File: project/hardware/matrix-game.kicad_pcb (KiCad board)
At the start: 2 copper layers, 11 parts, among them SW1 button_center, SW2 button_left, SW3 button_down, SW4 button_right, SW5 button_up, U1 NUCLEO-F042K6, U2 MAX7219, U3 SSD1306

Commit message: [project/hardware/layout] added custom footprint for LCD
Signed-off-by: Timon Burkard <timon.burkard@gwf.ch>
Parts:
- U3: footprint Connector_PinSocket_2.54mm:PinSocket_1x04_P2.54mm_Vertical -> Custom_Library:LCD_I2C
- moved U3 26.9 mm to (195.0, 121.0)
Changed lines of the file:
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@@
 		)
 	)
-	(footprint "Connector_PinSocket_2.54mm:PinSocket_1x04_P2.54mm_Vertical"
+	(footprint "Custom_Library:LCD_I2C"
 		(layer "F.Cu")
-		(at 168.09 120.35)
-		(descr "Through hole straight socket strip, 1x04, 2.54mm pitch, single row (from Kicad 4.0.7), script generated")
-		(tags "Through hole socket strip THT 1x04 2.54mm single row")
+		(at 195 121)
 		(property "Reference" "U3"
-			(at 0 -2.77 0)
-			(layer "F.SilkS")
-			(effects
-				(font
-					(size 1 1)
-					(thickness 0.15)
+			(at 0 -0.5 0)
+			(unlocked yes)
+			(layer "F.SilkS")
+			(effects
+				(font
+					(size 1 1)
+					(thickness 0.1)
 				)
 			)
 		)
 		(property "Value" "SSD1306"
-			(at 0 10.39 0)
-			(layer "F.Fab")
-			(effects
-				(font
-					(size 1 1)
-					(thickness 0.15)
-				)
-			)
-		)
-		(property "Footprint" "Connector_PinSocket_2.54mm:PinSocket_1x04_P2.54mm_Vertical"
+			(at 0 1 0)
+			(unlocked yes)
+			(layer "F.Fab")
+			(effects
+				(font
+					(size 1 1)
+					(thickness 0.15)
+				)
+			)
+		)
+		(property "Footprint" "Custom_Library:LCD_I2C"
 			(at 0 0 0)
 			(unlocked yes)
@@
 			(effects
 				(font
-					(size 1.27 1.27)
+					(size 1 1)
 					(thickness 0.15)
 				)
@@
 			(effects
 				(font
-					(size 1.27 1.27)
+					(size 1 1)
 					(thickness 0.15)
 				)
@@
 			(effects
 				(font
-					(size 1.27 1.27)
+					(size 1 1)
 					(thickness 0.15)
 				)
@@
 		(attr through_hole)
 		(fp_line
-			(start -1.33 1.27)
-			(end -1.33 8.95)
-			(stroke
-				(width 0.12)
-				(type solid)
-			)
-			(layer "F.SilkS")
-		)
-		(fp_line
-			(start -1.33 1.27)
-			(end 1.33 1.27)
-			(stroke
-				(width 0.12)
-				(type solid)
-			)
-			(layer "F.SilkS")
-		)
-		(fp_line
-			(start -1.33 8.95)
-			(end 1.33 8.95)
-			(stroke
-				(width 0.12)
-				(type solid)
-			)
-			(layer "F.SilkS")
-		)
-		(fp_line
-			(start 0 -1.33)
-			(end 1.33 -1.33)
-			(stroke
-				(width 0.12)
-				(type solid)
-			)
-			(layer "F.SilkS")
-		)
-		(fp_line
-			(start 1.33 -1.33)
-			(end 1.33 0)
-			(stroke
-				(width 0.12)
-				(type solid)
-			)
-			(layer "F.SilkS")
-		)
-		(fp_line
-			(start 1.33 1.27)
-			(end 1.33 8.95)
-			(stroke
-				(width 0.12)
-				(type solid)
-			)
-			(layer "F.SilkS")
-		)
-		(fp_line
-			(start -1.8 -1.8)
-			(end 1.75 -1.8)
-			(stroke
-				(width 0.05)
-				(type solid)
-			)
-			(layer "F.CrtYd")
-		)
-		(fp_line
-			(start -1.8 9.4)
-			(end -1.8 -1.8)
-			(stroke
-				(width 0.05)
-				(type solid)
-			)
-			(layer "F.CrtYd")
-		)
-		(fp_line
-			(start 1.75 -1.8)
-			(end 1.75 9.4)
-			(stroke
-				(width 0.05)
-				(type solid)
-			)
-			(layer "F.CrtYd")
-		)
-		(fp_line
-			(start 1.75 9.4)
-			(end -1.8 9.4)
-			(stroke
-				(width 0.05)
-				(type solid)
-			)
-			(layer "F.CrtYd")
-		)
-		(fp_line
-			(start -1.27 -1.27)
-			(end 0.635 -1.27)
-			(stroke
-				(width 0.1)
-				(type solid)
-			)
-			(layer "F.Fab")
-		)
-		(fp_line
-			(start -1.27 8.89)
-			(end -1.27 -1.27)
-			(stroke
-				(width 0.1)
-				(type solid)
-			)
-			(layer "F.Fab")
-		)
-		(fp_line
-			(start 0.635 -1.27)
-			(end 1.27 -0.635)
-			(stroke
-				(width 0.1)
-				(type solid)
-			)
-			(layer "F.Fab")
-		)
-		(fp_line
-			(start 1.27 -0.635)
-			(end 1.27 8.89)
-			(stroke
-				(width 0.1)
-				(type solid)
-			)
-			(layer "F.Fab")
-		)
-		(fp_line
-			(start 1.27 8.89)
-			(end -1.27 8.89)
-			(stroke
-				(width 0.1)
-				(type solid)
-			)
-			(layer "F.Fab")
+			(start -13 -12)
+			(end 13 -12)
+			(stroke
+				(width 0.1)
+				(type default)
+			)
+			(layer "F.SilkS")
+		)
+		(fp_line
+			(start -13 14)
+			(end -13 -12)
+			(stroke
+				(width 0.1)
+				(type default)
+			)
+			(layer "F.SilkS")
+		)
+		(fp_line
+			(start 13 -12)
+			(end 13 14)
+			(stroke
+				(width 0.1)
+				(type default)
+			)
+			(layer "F.SilkS")
+		)
+		(fp_line
+			(start 13 14)
+			(end -13 14)
+			(stroke
+				(width 0.1)
+				(type default)
+			)
+			(layer "F.SilkS")
+		)
+		(fp_text user "SCL"
+			(at 1.778 -6.604 90)
+			(unlocked yes)
+			(layer "F.SilkS")
+			(effects
+				(font
+					(size 0.7 0.7)
+					(thickness 0.15)
+					(bold yes)
+				)
+				(justify left bottom)
+			)
+		)
+		(fp_text user "SDA"
+			(at 4.318 -6.604 90)
+			(unlocked yes)
+			(layer "F.SilkS")
+			(effects
+				(font
+					(size 0.7 0.7)
+					(thickness 0.15)
+					(bold yes)
+				)
+				(justify left bottom)
+			)
+		)
+		(fp_text user "GND"
+			(at -3.302 -6.35 90)
+			(unlocked yes)
+			(layer "F.SilkS")
+			(effects
+				(font
+					(size 0.7 0.7)
+					(thickness 0.15)
+					(bold yes)
+				)
+				(justify left bottom)
+			)
+		)
+		(fp_text user "VCC"
+			(at -0.762 -6.35 90)
+			(unlocked yes)
+			(layer "F.SilkS")
+			(effects
+				(font
+					(size 0.7 0.7)
+					(thickness 0.15)
+					(bold yes)
+				)
+				(justify left bottom)
+			)
 		)
 		(fp_text user "${REFERENCE}"
-			(at 0 3.81 90)
+			(at 0 2.5 0)
+			(unlocked yes)
 			(layer "F.Fab")
 			(effects
@@
 		)
 		(pad "1" thru_hole rect
-			(at 0 0)
-			(size 1.7 1.7)
-			(drill 1)
+			(at -3.81 -10.16)
+			(size 1.524 1.524)
+			(drill 0.762)
 			(layers "*.Cu" "*.Mask")
 			(remove_unused_layers no)
@@
 			(pintype "input")
 		)
-		(pad "2" thru_hole oval
-			(at 0 2.54)
-			(size 1.7 1.7)
-			(drill 1)
+		(pad "2" thru_hole circle
+			(at -1.27 -10.16)
+			(size 1.524 1.524)
+			(drill 0.762)
 			(layers "*.Cu" "*.Mask")
 			(remove_unused_layers no)
@@
 			(pintype "input")
 		)
-		(pad "3" thru_hole oval
-			(at 0 5.08)
-			(size 1.7 1.7)
-			(drill 1)
+		(pad "3" thru_hole circle
+			(at 1.27 -10.16)
+			(size 1.524 1.524)
+			(drill 0.762)
 			(layers "*.Cu" "*.Mask")
 			(remove_unused_layers no)
@@
 			(pintype "input")
 		)
-		(pad "4" thru_hole oval
-			(at 0 7.62)
-			(size 1.7 1.7)
-			(drill 1)
+		(pad "4" thru_hole circle
+			(at 3.81 -10.16)
+			(size 1.524 1.524)
+			(drill 0.762)
 			(layers "*.Cu" "*.Mask")
 			(remove_unused_layers no)
@@
 			(pintype "input")
 		)
-		(model "${KICAD8_3DMODEL_DIR}/Connector_PinSocket_2.54mm.3dshapes/PinSocket_1x04_P2.54mm_Vertical.wrl"
-			(offset
-				(xyz 0 0 0)
-			)
-			(scale
-				(xyz 1 1 1)
-			)
-			(rotate
-				(xyz 0 0 0)
-			)
-		)
+		(zone
+			(net 0)
+			(net_name "")
+			(layer "F.SilkS")
+			(hatch edge 0.5)
+			(connect_pads
+				(clearance 0)
+			)
+			(min_thickness 0.25)
+			(filled_areas_thickness no)
+			(keepout
+				(tracks allowed)
+				(vias allowed)
+				(pads not_allowed)
+				(copperpour allowed)
+				(footprints not_allowed)
+			)
+			(fill
+				(thermal_gap 0.5)
+				(thermal_bridge_width 0.5)
+			)
+			(polygon
+				(pts
+					(xy 182 109) (xy 208 109) (xy 208 135) (xy 182 135)
+				)
+			)
+		)

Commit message: [project/hardware/layout] started layouting
Signed-off-by: Timon Burkard <timon.burkard@gwf.ch>
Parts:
- moved SW2 96.3 mm to (112.0, 128.9), turned to 180 degrees
- moved SW1 94.7 mm to (126.0, 128.9), turned to 180 degrees
- moved SW3 90.7 mm to (119.5, 136.6)
- moved U3 67.3 mm to (170.8, 58.2)
- moved SW4 66.3 mm to (138.7, 128.9), turned to 180 degrees
- moved SW5 61.2 mm to (126.0, 117.5), turned to 180 degrees
- moved U1 31.3 mm to (178.6, 101.8), turned to 180 degrees
- moved U2 25.2 mm to (157.9, 77.5)
- moved BZ1 15.5 mm to (163.8, 121.9), turned to 180 degrees
- moved R1 5.16 mm to (166.1, 111.0), turned to 180 degrees
- moved D1 2.40 mm to (121.0, 76.0)
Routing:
- net Net-(U1-PA3/A2): track 0.00 -> 109.8 mm
- net +3.3V: track 0.00 -> 109.6 mm, vias 0 -> 28
- net Net-(U1-PB1/D6): track 0.00 -> 97.7 mm, vias 0 -> 1
- net Net-(D1-R3): track 0.00 -> 87.2 mm
- net Net-(D1-R5): track 0.00 -> 85.7 mm
- net Net-(D1-R7): track 0.00 -> 78.9 mm, vias 0 -> 1
- net Net-(U1-PA8/D9): track 0.00 -> 78.6 mm
- net Net-(D1-R6): track 0.00 -> 74.8 mm
- net Net-(U1-PB0/D3): track 0.00 -> 74.7 mm, vias 0 -> 1
- net Net-(D1-C2): track 0.00 -> 72.4 mm, vias 0 -> 1
- net Net-(D1-R8): track 0.00 -> 69.5 mm
- net Net-(U1-PA12/D2): track 0.00 -> 66.6 mm
- net Net-(D1-C3): track 0.00 -> 66.1 mm, vias 0 -> 3
- net Net-(D1-C5): track 0.00 -> 60.9 mm, vias 0 -> 2
- net Net-(U1-PA7/A6): track 0.00 -> 55.6 mm, vias 0 -> 1
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- added copper zone on B.Cu, net +3.3V
- added copper zone on F.Cu, net GND
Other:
- board outline added: 100 x 100 mm

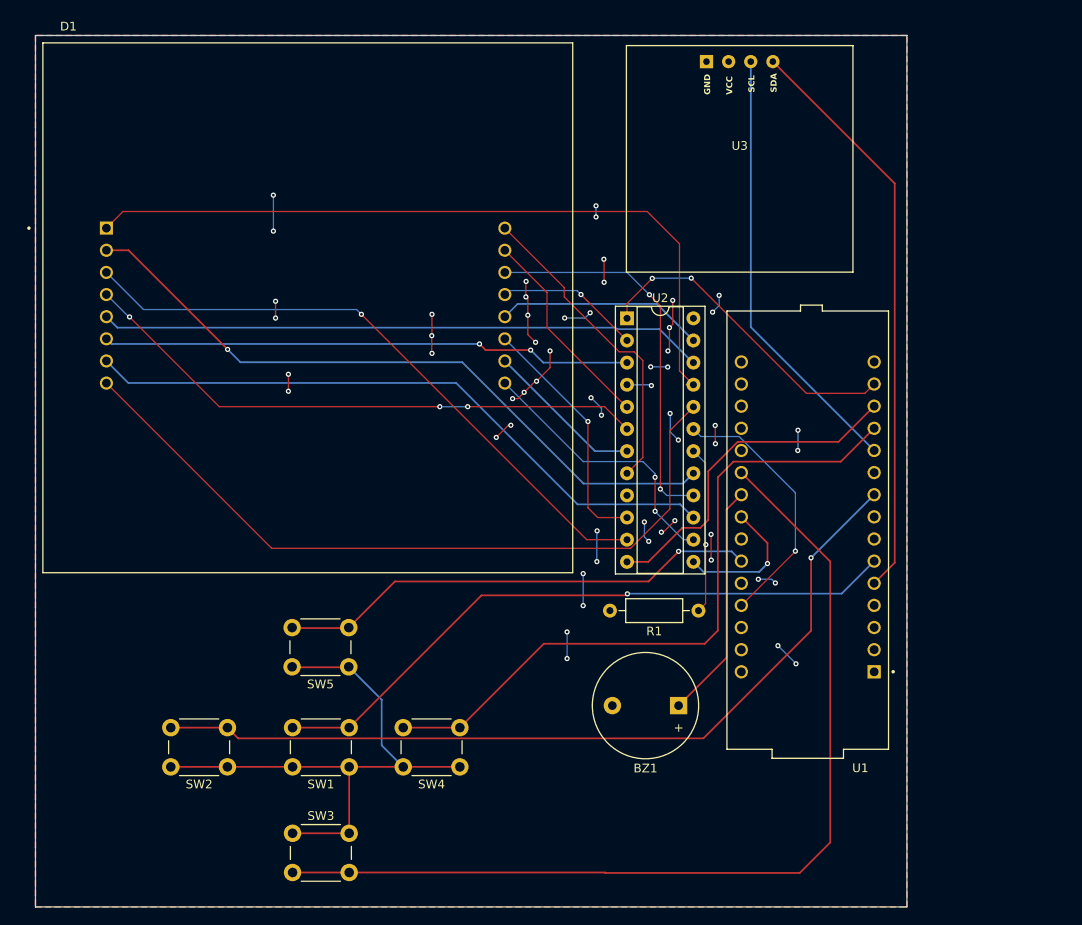
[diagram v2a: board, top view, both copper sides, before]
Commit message: [project/hardware/layout] set all tracks to 0.2 mm width
Signed-off-by: Timon Burkard <timon.burkard@gwf.ch>
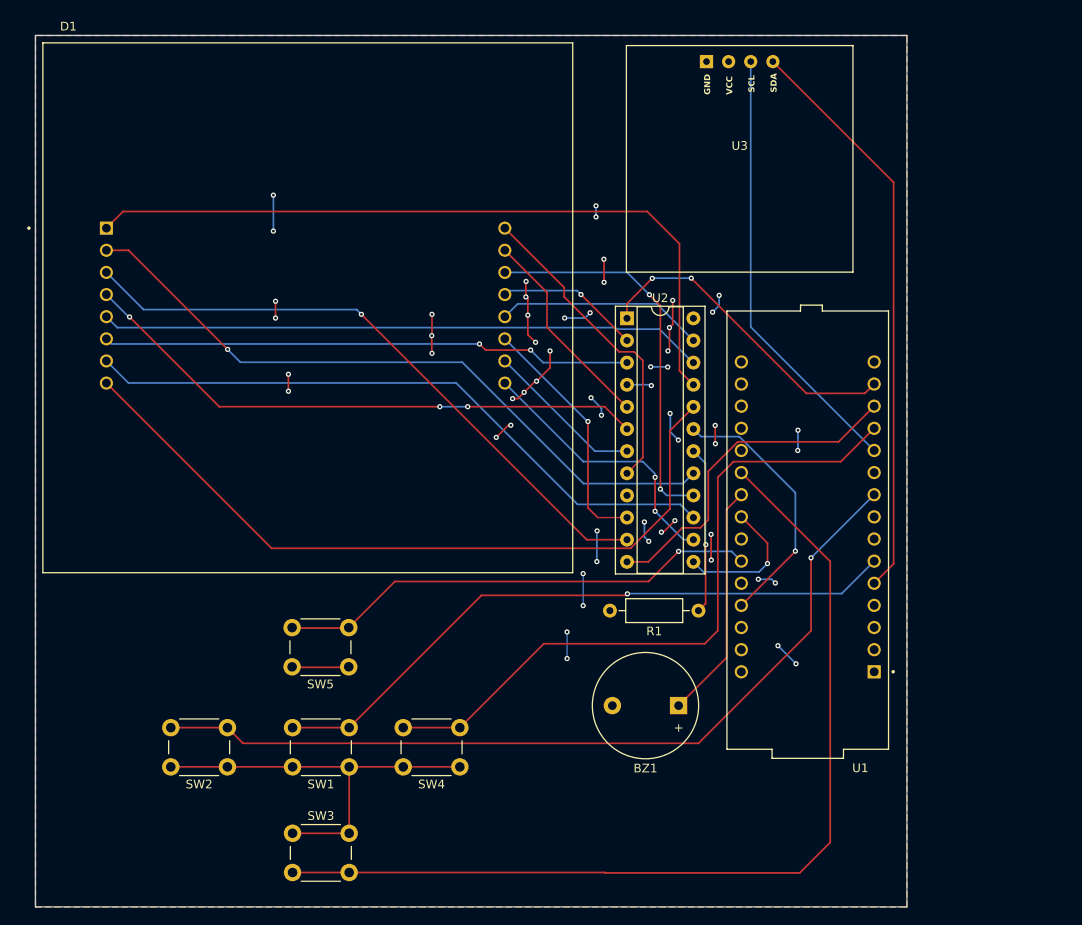
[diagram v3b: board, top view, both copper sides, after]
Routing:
- net +3.3V: track 109.6 -> 95.5 mm
- net Net-(D1-R5): track 85.7 -> 84.9 mm

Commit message: [project/hardware/layout] rotation of matrix LED
Signed-off-by: Timon Burkard <timon.burkard@gwf.ch>
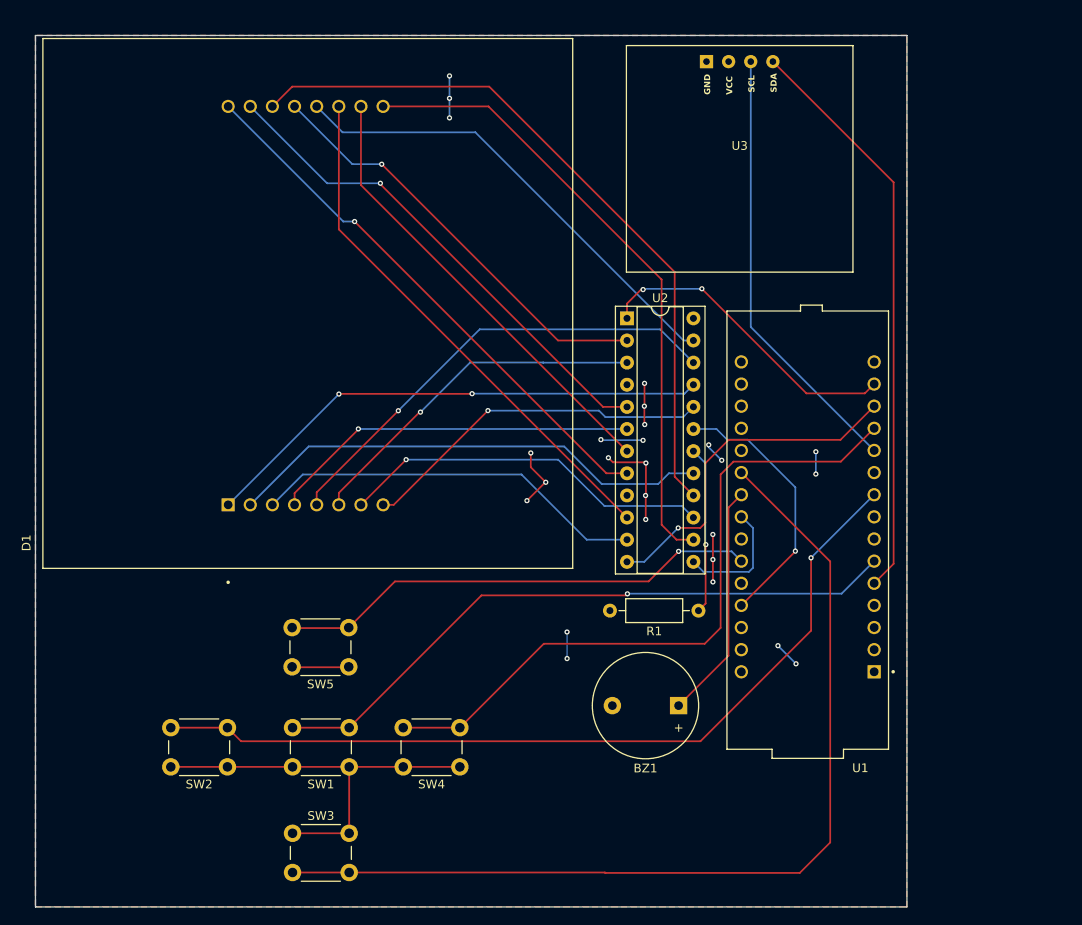
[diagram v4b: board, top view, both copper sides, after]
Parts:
- turned D1 to 90 degrees
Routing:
- net Net-(D1-R3): track 87.2 -> 40.9 mm, vias 0 -> 1
- net Net-(D1-R1): track 31.6 -> 72.7 mm, vias 2 -> 0
- net Net-(D1-R2): track 44.6 -> 82.4 mm, vias 2 -> 0
- net Net-(D1-C4): track 18.3 -> 52.2 mm
- net Net-(D1-C7): track 23.8 -> 57.6 mm, vias 0 -> 1
- net Net-(D1-C1): track 16.6 -> 49.3 mm
- net Net-(D1-C6): track 28.3 -> 60.9 mm, vias 1 -> 0
- net Net-(D1-R6): track 74.8 -> 43.1 mm, vias 0 -> 1
- net Net-(D1-R4): track 24.0 -> 54.4 mm
- net Net-(D1-C2): track 72.4 -> 45.2 mm, vias 1 -> 0
- net Net-(D1-C8): track 36.5 -> 63.2 mm, vias 0 -> 1
- net Net-(D1-R5): track 84.9 -> 59.1 mm, vias 0 -> 2
- net Net-(D1-C3): track 66.1 -> 42.6 mm, vias 3 -> 1
- net Net-(D1-R7): track 78.9 -> 55.9 mm, vias 1 -> 0
- net GND: track 41.6 -> 20.6 mm, vias 29 -> 13
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
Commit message: [project/hardware] added test points
Signed-off-by: Timon Burkard <timon.burkard@gwf.ch>
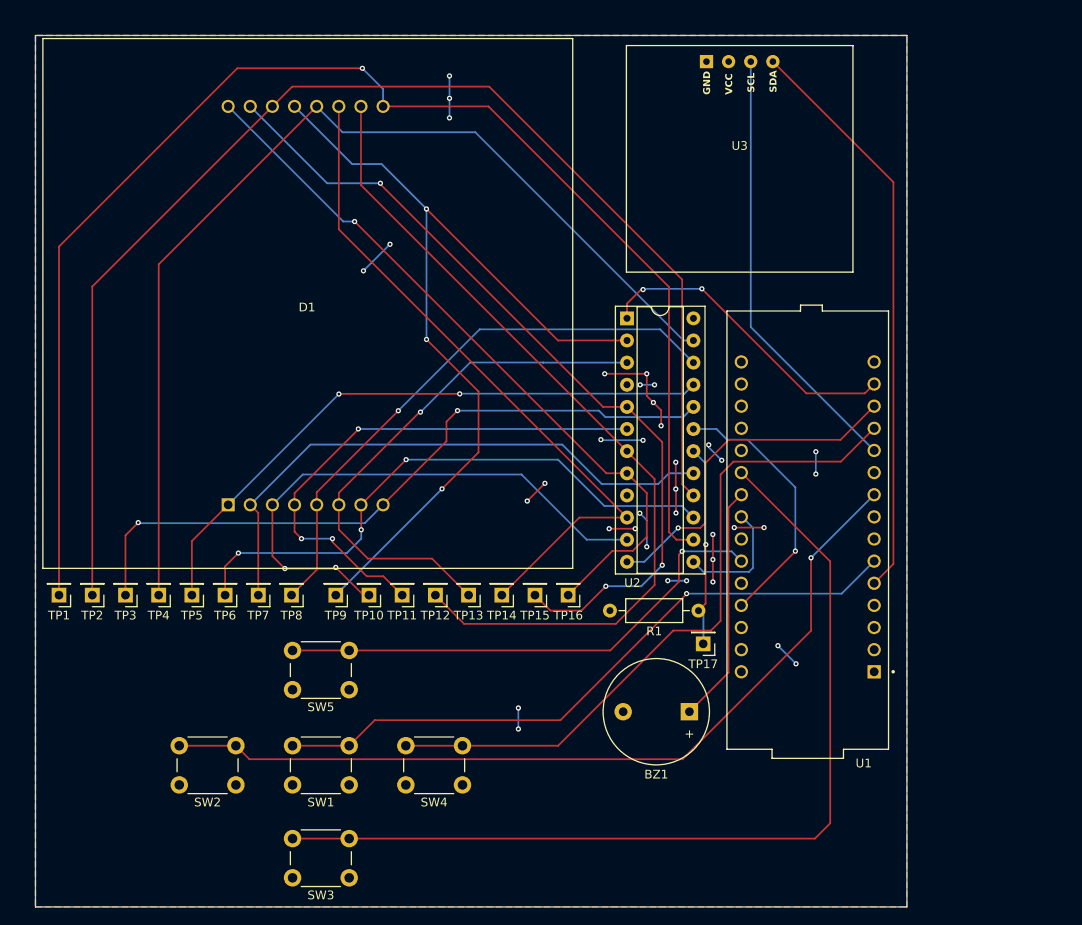
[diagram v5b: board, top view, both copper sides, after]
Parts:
- added TP1: TestPoint, Connector_PinHeader_2.54mm:PinHeader_1x01_P2.54mm_Vertical, F.Cu at (92.7, 109.2)
- added TP10: TestPoint, Connector_PinHeader_2.54mm:PinHeader_1x01_P2.54mm_Vertical, F.Cu at (128.3, 109.2)
- added TP11: TestPoint, Connector_PinHeader_2.54mm:PinHeader_1x01_P2.54mm_Vertical, F.Cu at (132.1, 109.2)
- added TP12: TestPoint, Connector_PinHeader_2.54mm:PinHeader_1x01_P2.54mm_Vertical, F.Cu at (135.9, 109.2)
- added TP13: TestPoint, Connector_PinHeader_2.54mm:PinHeader_1x01_P2.54mm_Vertical, F.Cu at (139.7, 109.2)
- added TP14: TestPoint, Connector_PinHeader_2.54mm:PinHeader_1x01_P2.54mm_Vertical, F.Cu at (143.5, 109.2)
- added TP15: TestPoint, Connector_PinHeader_2.54mm:PinHeader_1x01_P2.54mm_Vertical, F.Cu at (147.3, 109.2)
- added TP16: TestPoint, Connector_PinHeader_2.54mm:PinHeader_1x01_P2.54mm_Vertical, F.Cu at (151.1, 109.2)
- added TP17: TestPoint, Connector_PinHeader_2.54mm:PinHeader_1x01_P2.54mm_Vertical, F.Cu at (166.6, 114.8)
- added TP2: TestPoint, Connector_PinHeader_2.54mm:PinHeader_1x01_P2.54mm_Vertical, F.Cu at (96.5, 109.2)
- added TP3: TestPoint, Connector_PinHeader_2.54mm:PinHeader_1x01_P2.54mm_Vertical, F.Cu at (100.3, 109.2)
- added TP4: TestPoint, Connector_PinHeader_2.54mm:PinHeader_1x01_P2.54mm_Vertical, F.Cu at (104.1, 109.2)
- added TP5: TestPoint, Connector_PinHeader_2.54mm:PinHeader_1x01_P2.54mm_Vertical, F.Cu at (108.0, 109.2)
- added TP6: TestPoint, Connector_PinHeader_2.54mm:PinHeader_1x01_P2.54mm_Vertical, F.Cu at (111.8, 109.2)
- added TP7: TestPoint, Connector_PinHeader_2.54mm:PinHeader_1x01_P2.54mm_Vertical, F.Cu at (115.6, 109.2)
- added TP8: TestPoint, Connector_PinHeader_2.54mm:PinHeader_1x01_P2.54mm_Vertical, F.Cu at (119.4, 109.2)
- added TP9: TestPoint, Connector_PinHeader_2.54mm:PinHeader_1x01_P2.54mm_Vertical, F.Cu at (124.5, 109.2)
- moved SW3 8.27 mm to (126.0, 141.7), turned to 180 degrees
- moved SW5 2.62 mm to (126.0, 120.1)
- moved SW2 2.29 mm to (113.0, 131.0)
- moved SW4 2.09 mm to (139.0, 131.0)
- moved SW1 2.07 mm to (126.0, 131.0)
- moved BZ1 1.42 mm to (165.0, 122.6)
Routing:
- net Net-(D1-R1): track 72.7 -> 161.3 mm, vias 0 -> 1
- net Net-(D1-R2): track 82.4 -> 147.1 mm
- net Net-(D1-R4): track 54.4 -> 117.9 mm
- net Net-(D1-C1): track 49.3 -> 102.9 mm, vias 1 -> 3
- net +3.3V: track 82.2 -> 32.1 mm, vias 13 -> 16
- net Net-(D1-C4): track 52.2 -> 97.3 mm
- net Net-(D1-R3): track 40.9 -> 80.2 mm, vias 1 -> 2
- net Net-(D1-C7): track 57.6 -> 95.0 mm, vias 1 -> 3
- net Net-(D1-R6): track 43.1 -> 67.2 mm, vias 1 -> 3
- net Net-(D1-C5): track 40.6 -> 61.5 mm
- net Net-(D1-C8): track 63.2 -> 83.2 mm
- net Net-(D1-C2): track 45.2 -> 64.2 mm, vias 0 -> 2
- net Net-(D1-C3): track 42.6 -> 61.3 mm, vias 1 -> 3
- net Net-(D1-C6): track 60.9 -> 78.9 mm
- net Net-(D1-R5): track 59.1 -> 71.2 mm
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
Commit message: [project/hardware] added jumper for buzzer
Signed-off-by: Timon Burkard <timon.burkard@gwf.ch>
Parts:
- added JP1: Jumper_2_Bridged, Connector_PinHeader_2.54mm:PinHeader_1x02_P2.54mm_Vertical, F.Cu at (162.9, 132.4)
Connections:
- U1 pad CN4_9: Net-(BZ1-+) -> Net-(JP1-A)
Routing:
- net Net-(JP1-A): track 0.00 -> 38.1 mm
- net Net-(BZ1-+): track 27.9 -> 12.3 mm
- net Net-(U1-PB1/D6): track 97.9 -> 109.5 mm
- net GND: track 32.4 -> 34.9 mm, vias 21 -> 23

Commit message: [project/hardware] added capacitors for LCD and MAX7219, logo and version
Signed-off-by: Timon Burkard <timon.burkard@gwf.ch>
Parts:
- added C1: 100n, Capacitor_THT:C_Disc_D3.0mm_W2.0mm_P2.50mm, B.Cu at (163.5, 50.4)
- added C2: 100n, Capacitor_THT:C_Disc_D3.0mm_W2.0mm_P2.50mm, B.Cu at (168.2, 90.1)
- added G***: LOGO, LOGO, F.Cu at (157.0, 141.2)
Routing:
- net GND: track 34.9 -> 49.7 mm, vias 23 -> 26
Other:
- board text added: "Schnupperlehre Elektroniker/in Projekt Matrix-Game v1.0"
- board text added: "swiss.smart.simple."
